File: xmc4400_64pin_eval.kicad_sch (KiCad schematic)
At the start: 47 parts, among them IC1 TLV75533PDBVR, IC6 SN65HVD230DR, J11 SWD & JTAG, J17 VCP, J3 IO_1, J4 IO_2, J5 POW, J6 CAN, J7 Vbat, U5 XMC440x-LQFP64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

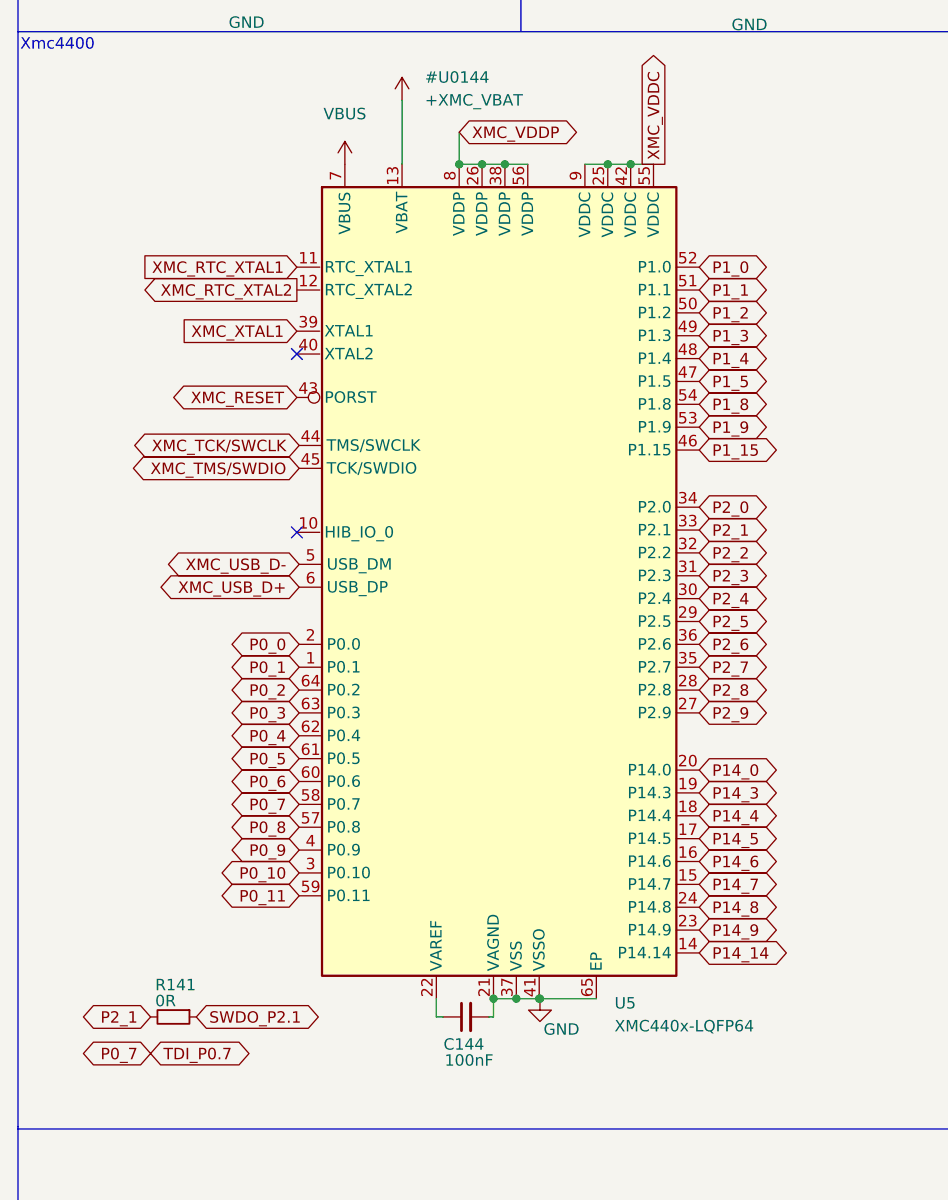
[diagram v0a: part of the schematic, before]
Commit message: Fix swd pins
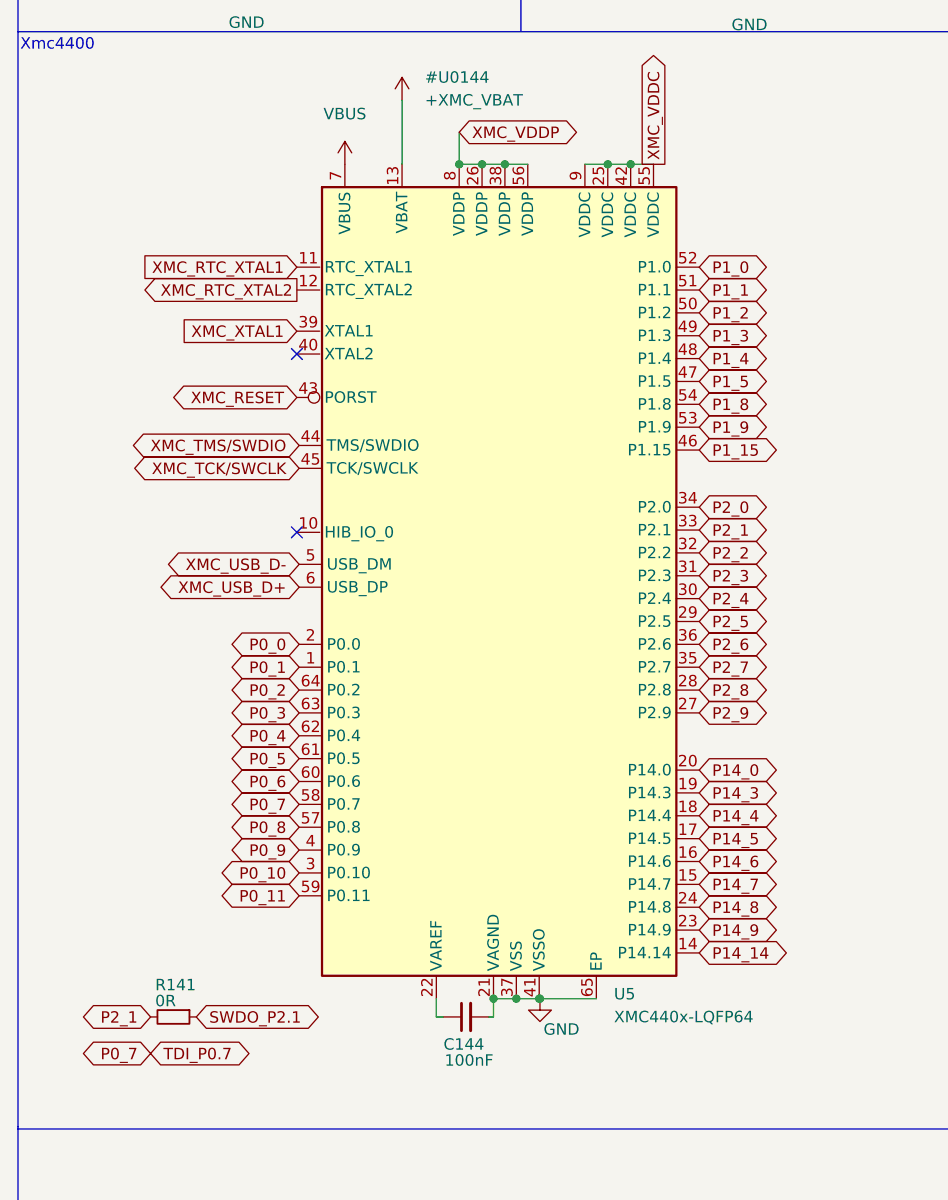
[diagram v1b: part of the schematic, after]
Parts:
- U5: symbol xmc:XMC440x-LQFP64 -> xmc:XMC440x-64
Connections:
- net XMC_TCK/SWCLK: now also U5.45 (TCK/SWCLK); no longer U5.44 (TMS/SWCLK)
- net XMC_TMS/SWDIO: now also U5.44 (TMS/SWDIO); no longer U5.45 (TCK/SWDIO)
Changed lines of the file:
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@@
+    )
+  )
+  (global_label "XMC_TMS{slash}SWDIO" (shape tri_state) (at 43.942 76.454 180) (fields_autoplaced)
+    (effects (font (size 1.27 1.27)) (justify right))
+    (property "Intersheetrefs" "${INTERSHEET_REFS}" (at 25.8051 76.5334 0)
+      (effects (font (size 1.27 1.27)) (justify right) hide)
     )
   )
@@
     )
   )
-  (global_label "XMC_TMS{slash}SWDIO" (shape tri_state) (at 43.942 78.994 180) (fields_autoplaced)
-    (effects (font (size 1.27 1.27)) (justify right))
-    (property "Intersheetrefs" "${INTERSHEET_REFS}" (at 25.8051 79.0734 0)
-      (effects (font (size 1.27 1.27)) (justify right) hide)
-    )
-  )
   (global_label "P2_1" (shape bidirectional) (at 141.224 128.524 180) (fields_autoplaced)
     (effects (font (size 1.27 1.27)) (justify right))
@@
     )
   )
-  (global_label "XMC_TCK{slash}SWCLK" (shape tri_state) (at 43.942 76.454 180) (fields_autoplaced)
-    (effects (font (size 1.27 1.27)) (justify right))
-    (property "Intersheetrefs" "${INTERSHEET_REFS}" (at 25.5632 76.3746 0)
-      (effects (font (size 1.27 1.27)) (justify right) hide)
-    )
-  )
   (global_label "XMC_VDDP" (shape bidirectional) (at 247.396 17.78 180) (fields_autoplaced)
     (effects (font (size 1.27 1.27)) (justify right))
@@
     (effects (font (size 1.27 1.27)) (justify right))
     (property "Intersheetrefs" "${INTERSHEET_REFS}" (at 131.3408 110.744 0)
+      (effects (font (size 1.27 1.27)) (justify right) hide)
+    )
+  )
+  (global_label "XMC_TCK{slash}SWCLK" (shape tri_state) (at 43.942 78.994 180) (fields_autoplaced)
+    (effects (font (size 1.27 1.27)) (justify right))
+    (property "Intersheetrefs" "${INTERSHEET_REFS}" (at 25.5632 78.9146 0)
       (effects (font (size 1.27 1.27)) (justify right) hide)
     )
@@
     )
   )
-  (symbol (lib_id "xmc:XMC440x-LQFP64") (at 66.802 150.622 0) (unit 1)
+  (symbol (lib_id "xmc:XMC440x-64") (at 65.786 96.266 0) (unit 1)
     (in_bom yes) (on_board yes) (dnp no) (fields_autoplaced)
-    (property "Reference" "U5" (at 78.9814 138.43 0)
-      (effects (font (size 1.27 1.27)) (justify left))
-    )
-    (property "Value" "XMC440x-LQFP64" (at 78.9814 140.97 0)
-      (effects (font (size 1.27 1.27)) (justify left))
-    )
-    (property "Footprint" "Package_QFP:LQFP-64-1EP_10x10mm_P0.5mm_EP6.5x6.5mm" (at 66.802 150.622 0)
-      (effects (font (size 1.27 1.27)) hide)
-    )
-    (property "Datasheet" "https://www.infineon.com/dgdl/Infineon-XMC4400-DS-v01_03-EN.pdf?fileId=5546d462696dbf12016981795855391d" (at 66.802 154.432 0)
-      (effects (font (size 1.27 1.27)) hide)
-    )
-    (property "Code" "XMC4400F64F512BAXQMA1" (at 66.802 150.622 0)
-      (effects (font (size 1.27 1.27)) hide)
-    )
-    (property "Stock" "https://www.digikey.com/en/products/detail/infineon-technologies/XMC4400F64F512BAXQMA1/6250127" (at 66.802 150.622 0)
-      (effects (font (size 1.27 1.27)) hide)
-    )
-    (pin "1")
+    (property "Reference" "U5" (at 78.9179 137.414 0)
+      (effects (font (size 1.27 1.27)) (justify left))
+    )
+    (property "Value" "XMC440x-LQFP64" (at 78.9179 139.954 0)
+      (effects (font (size 1.27 1.27)) (justify left))
+    )
+    (property "Footprint" "Package_QFP:LQFP-64-1EP_10x10mm_P0.5mm_EP6.5x6.5mm" (at 107.696 35.56 0)
+      (effects (font (size 1.27 1.27)) hide)
+    )
+    (property "Datasheet" "https://www.infineon.com/dgdl/Infineon-XMC4400-DS-v01_03-EN.pdf?fileId=5546d462696dbf12016981795855391d" (at 107.696 35.56 0)
+      (effects (font (size 1.27 1.27)) hide)
+    )
+    (property "Code" "XMC4400F64F512BAXQMA1" (at 65.786 96.266 0)
+      (effects (font (size 1.27 1.27)) hide)
+    )
+    (property "Stock" "https://www.digikey.com/en/products/detail/infineon-technologies/XMC4400F64F512BAXQMA1/6250127" (at 78.9179 142.494 0)
+      (effects (font (size 1.27 1.27)) (justify left) hide)
+    )
+    (pin "1")
